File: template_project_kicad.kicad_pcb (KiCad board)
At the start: 2 copper layers, 53.3 x 50.8 mm, 5 parts

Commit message: Forced minor change to trigger CICD
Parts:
- moved PS1 0.25 mm to (115.9, 87.6)
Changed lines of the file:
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@@
   )
   (footprint "twyleg-voltage-regulators:Polulu-S13V30F5" (layer "F.Cu")
-    (at 115.645 87.555)
+    (at 115.899 87.555)
     (property "Sheetfile" "template_project_kicad.kicad_sch")
     (property "Sheetname" "")

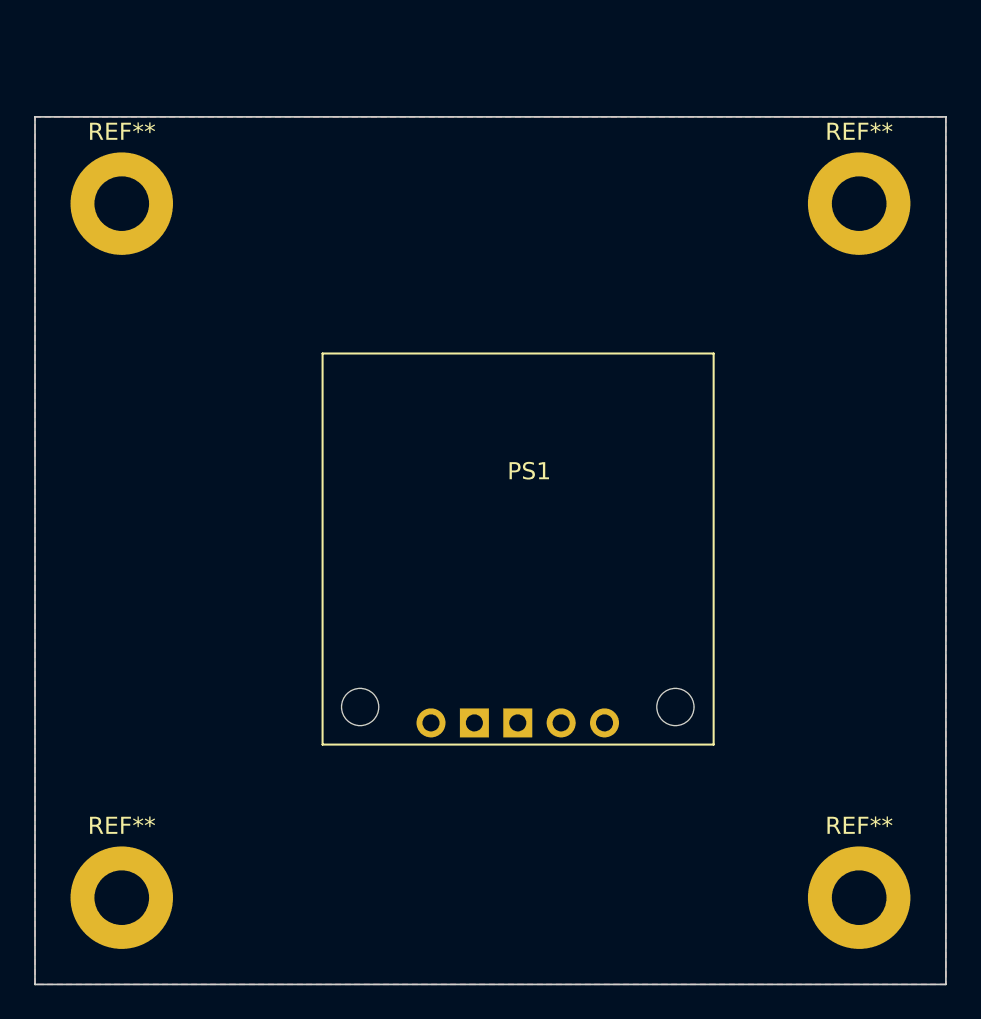
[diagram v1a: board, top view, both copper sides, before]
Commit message: Updated paths and replaced voltage regulator with raspberry pi pico in template
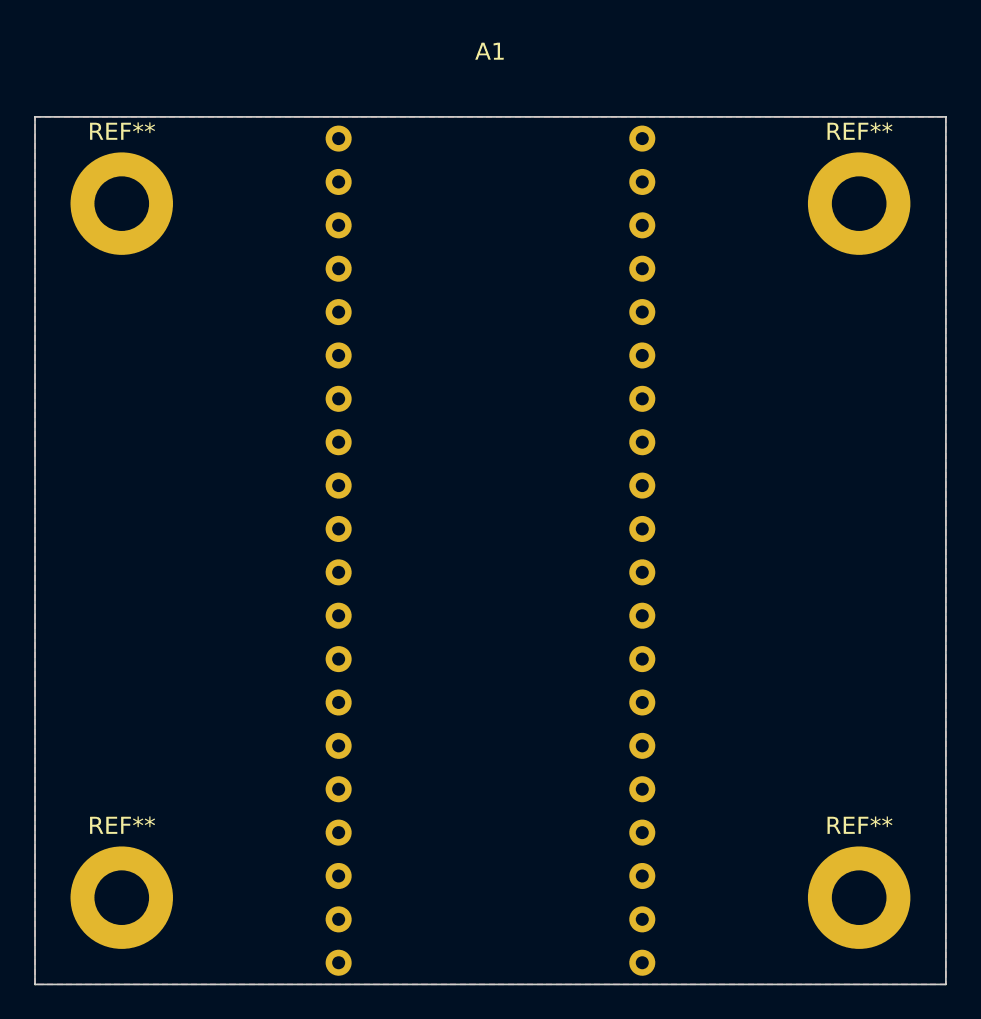
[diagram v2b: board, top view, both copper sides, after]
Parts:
- removed PS1: Polulu-S13V30F5, twyleg-voltage-regulators:Polulu-S13V30F5
- added A1: RaspberryPi-Pico, twyleg-board-connectors:RaspberryPiPico-THT-Dev, F.Cu at (125.7, 52.1)
